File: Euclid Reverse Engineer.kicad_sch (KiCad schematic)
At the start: 9 parts, among them J1 Conn_01x04_Female

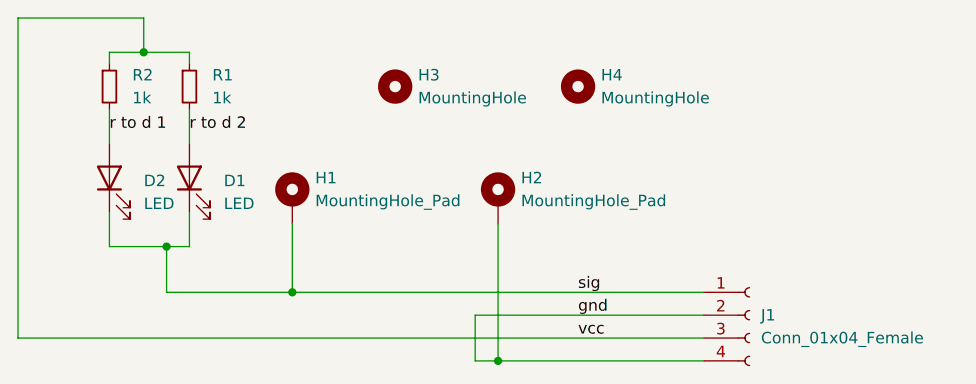
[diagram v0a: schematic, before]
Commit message: Fixing sdpt spacing
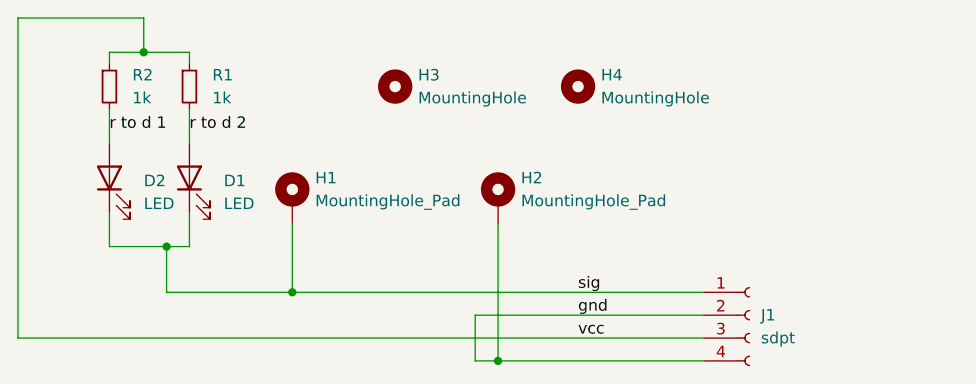
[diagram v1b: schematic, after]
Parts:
- J1: value Conn_01x04_Female -> sdpt
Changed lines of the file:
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@@
     (pin "2")
-  )
-  (symbol (lib_id "Connector:Conn_01x04_Female") (at 171.45 121.92 0) (unit 1)
-    (in_bom yes) (on_board yes) (fields_autoplaced)
-    (property "Reference" "J1" (id 0) (at 172.72 121.9199 0)
-      (effects (font (size 1.27 1.27)) (justify left))
-    )
-    (property "Value" "Conn_01x04_Female" (id 1) (at 172.72 124.4599 0)
-      (effects (font (size 1.27 1.27)) (justify left))
-    )
-    (property "Footprint" "custom:sdpt" (id 2) (at 171.45 121.92 0)
-      (effects (font (size 1.27 1.27)) hide)
-    )
-    (property "Datasheet" "~" (id 3) (at 171.45 121.92 0)
-      (effects (font (size 1.27 1.27)) hide)
-    )
-    (pin "1")
-    (pin "2")
-    (pin "3")
-    (pin "4")
   )
   (symbol (lib_id "Mechanical:MountingHole_Pad") (at 120.65 109.22 0) (unit 1)
@@
     )
     (pin "1")
+  )
+  (symbol (lib_id "Connector:Conn_01x04_Female") (at 171.45 121.92 0) (unit 1)
+    (in_bom yes) (on_board yes) (fields_autoplaced)
+    (property "Reference" "J1" (id 0) (at 172.72 121.9199 0)
+      (effects (font (size 1.27 1.27)) (justify left))
+    )
+    (property "Value" "sdpt" (id 1) (at 172.72 124.4599 0)
+      (effects (font (size 1.27 1.27)) (justify left))
+    )
+    (property "Footprint" "custom:sdpt" (id 2) (at 171.45 121.92 0)
+      (effects (font (size 1.27 1.27)) hide)
+    )
+    (property "Datasheet" "~" (id 3) (at 171.45 121.92 0)
+      (effects (font (size 1.27 1.27)) hide)
+    )
+    (pin "1")
+    (pin "2")
+    (pin "3")
+    (pin "4")
   )
   (symbol (lib_id "Device:R_Small") (at 109.22 96.52 0) (unit 1)
@@
       (reference "H4") (unit 1) (value "MountingHole") (footprint "MountingHole:MountingHole_2.1mm")
     )
-    (path "/8f8d8639-cc3a-4088-8a42-c991f15ed73d"
-      (reference "J1") (unit 1) (value "Conn_01x04_Female") (footprint "custom:sdpt")
+    (path "/d66ba902-8561-4ab4-9fd4-0f6e5c330a84"
+      (reference "J1") (unit 1) (value "sdpt") (footprint "custom:sdpt")
     )
     (path "/da0bcd5e-2313-44b1-8499-1ecd8faa59a6"
